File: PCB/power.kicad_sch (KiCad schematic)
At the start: 45 parts, among them Q1 AO3401A, U5 LM317_SOT-223, U6 LM317_SOT-223, U7 TPS65131RGE, U8 LM317_SOT-223, U9 LM337_SOT223

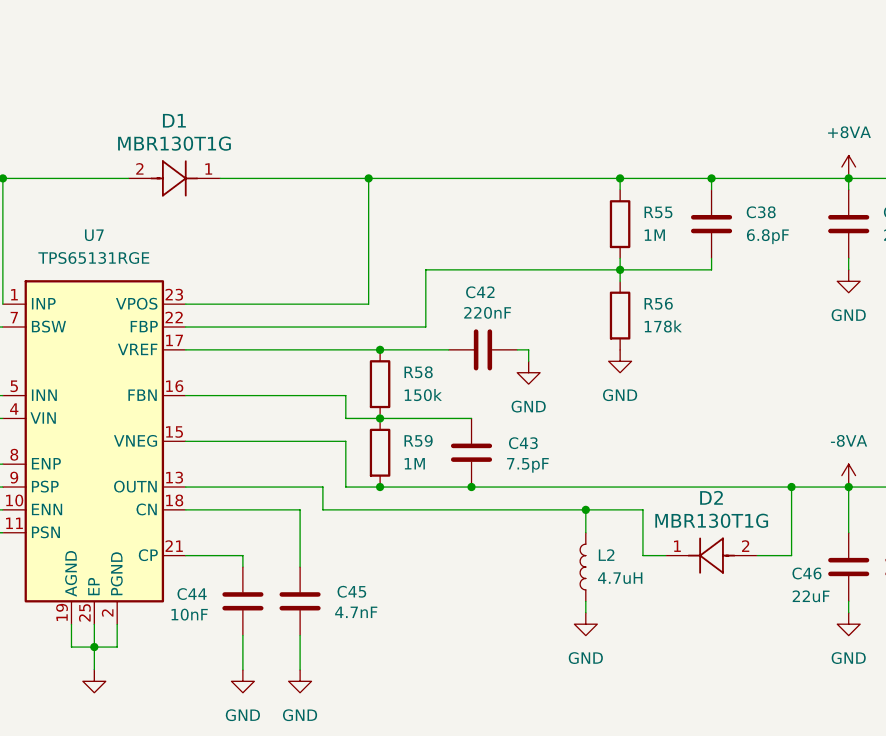
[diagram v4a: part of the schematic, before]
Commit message: Basic routing finished. Still missing some optimizing steps and DRC
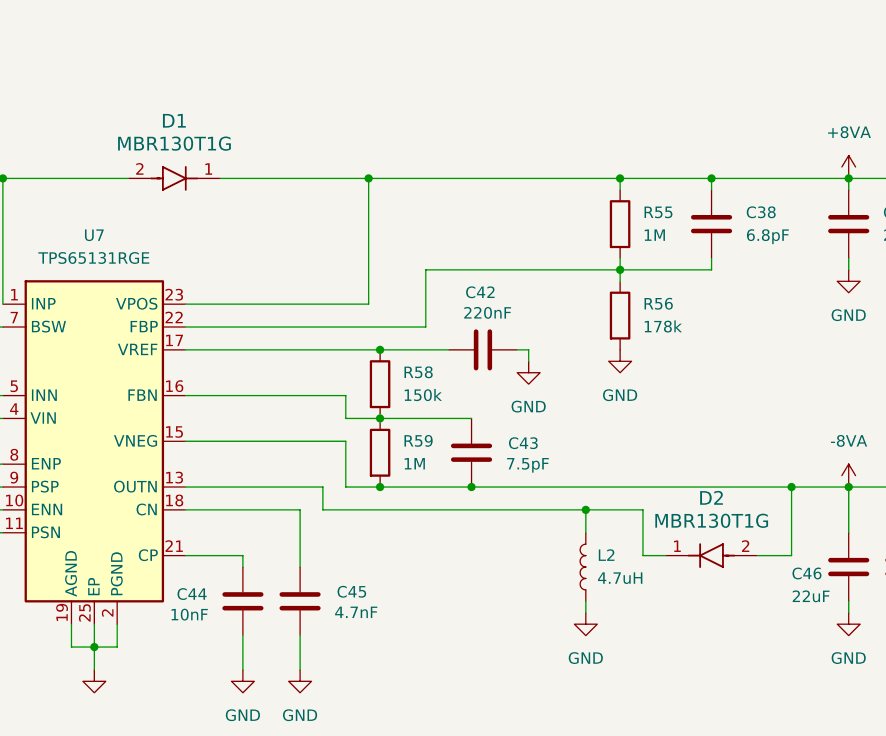
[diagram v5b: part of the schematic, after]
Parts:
- D1, D2: footprint SOD-123_425-04_ONS -> mahaudio KiCad Library:SOD-123_425-04_ONS; symbol mahaudio_kicad_lib:MBR130T1G -> mahaudio KiCad Library:MBR130T1G
- L1, L2: footprint LIB:WE-MAPI_4030 -> mahaudio KiCad Library:WE-MAPI_4030
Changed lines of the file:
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@@
 			)
 		)
-		(symbol "mahaudio_kicad_lib:MBR130T1G"
+		(symbol "mahaudio KiCad Library:MBR130T1G"
 			(pin_names
 				(offset 0.254)
@@
 			(in_bom yes)
 			(on_board yes)
-			(property "Reference" "CR"
-				(at 5.08 4.445 0)
+			(property "Reference" "D"
+				(at 5.08 -6.35 0)
 				(effects
 					(font
@@
 				)
 			)
-			(property "Footprint" "SOD-123_425-04_ONS"
+			(property "Footprint" "mahaudio KiCad Library:SOD-123_425-04_ONS"
 				(at 0 0 0)
 				(effects
@@
 				(polyline
 					(pts
-						(xy 3.81 -1.905) (xy 6.35 0)
+						(xy 3.81 -1.27) (xy 6.35 0)
 					)
 					(stroke
@@
 				(polyline
 					(pts
-						(xy 3.81 1.905) (xy 3.81 -1.905)
+						(xy 3.81 1.27) (xy 3.81 -1.27)
 					)
 					(stroke
@@
 				(polyline
 					(pts
-						(xy 6.35 -1.905) (xy 6.35 1.905)
+						(xy 6.35 -1.27) (xy 6.35 1.27)
 					)
 					(stroke
@@
 				(polyline
 					(pts
-						(xy 6.35 0) (xy 3.81 1.905)
+						(xy 6.35 0) (xy 3.81 1.27)
 					)
 					(stroke
@@
 			)
 		)
-		(property "Footprint" "LIB:WE-MAPI_4030"
+		(property "Footprint" "mahaudio KiCad Library:WE-MAPI_4030"
 			(at 156.21 76.2 0)
 			(effects
@@
 	)
 	(symbol
-		(lib_id "mahaudio_kicad_lib:MBR130T1G")
+		(lib_id "mahaudio KiCad Library:MBR130T1G")
 		(at 105.41 33.02 0)
 		(unit 1)
@@
 			)
 		)
-		(property "Footprint" "SOD-123_425-04_ONS"
+		(property "Footprint" "mahaudio KiCad Library:SOD-123_425-04_ONS"
 			(at 105.41 33.02 0)
 			(effects
@@
 	)
 	(symbol
-		(lib_id "mahaudio_kicad_lib:MBR130T1G")
+		(lib_id "mahaudio KiCad Library:MBR130T1G")
 		(at 175.26 74.93 180)
 		(unit 1)
@@
 			)
 		)
-		(property "Footprint" "SOD-123_425-04_ONS"
+		(property "Footprint" "mahaudio KiCad Library:SOD-123_425-04_ONS"
 			(at 175.26 74.93 0)
 			(effects
@@
 			)
 		)
-		(property "Footprint" "LIB:WE-MAPI_4030"
+		(property "Footprint" "mahaudio KiCad Library:WE-MAPI_4030"
 			(at 85.09 33.02 0)
 			(effects

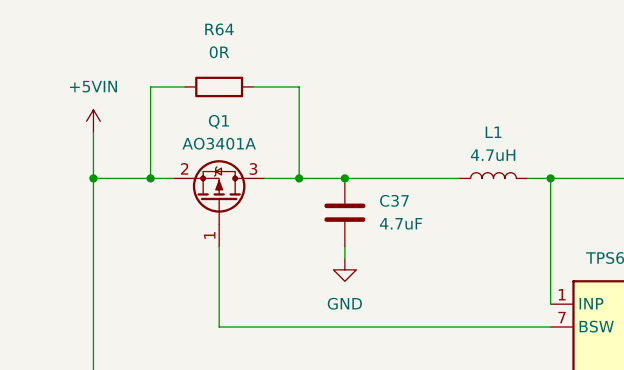
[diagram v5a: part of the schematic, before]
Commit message: Routing revised, added some missing parameters to components
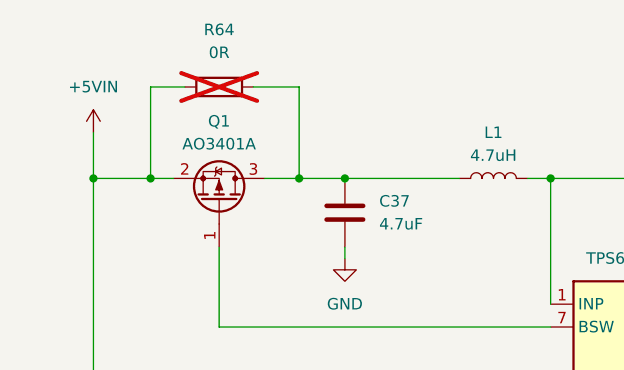
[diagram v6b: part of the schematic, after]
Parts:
- C21, C23, C24, C30, C44, C45, C50, C51: Tolerance (none) -> 10%; Voltage (none) -> 16V
- C22, C29, C41, C42, C48, C49: Tolerance (none) -> 10%; Voltage (none) -> 25V
- C37, C39, C40, C46, C47: Tolerance (none) -> 10%; Voltage (none) -> 10V
- C38, C43: Tolerance (none) -> 0.1pF; Voltage (none) -> 50V
- L1, L2: Tolerance (none) -> 20%
- R43, R44, R53, R54, R55, R56, R58, R59, R62, R63: Tolerance (none) -> 1%
- R57, R60, R61: Tolerance (none) -> 5%
- R64: now not fitted

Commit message: Updated PCB with digital traxce suggestions. Added JLCPCB Pns
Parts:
- C21, C23, C24, C30, C50, C51: JLCPCBPn (none) -> C15849
- C22, C29, C41, C48, C49: JLCPCBPn (none) -> C1525; Voltage 25V -> 16V
- C37, C40: JLCPCBPn (none) -> C19666
- C38: JLCPCBPn (none) -> C88896
- C39, C46, C47: JLCPCBPn (none) -> C84419
- C42: JLCPCBPn (none) -> C16772; Voltage 25V -> 16V
- C43: JLCPCBPn (none) -> C88938
- C44: JLCPCBPn (none) -> C15195; Voltage 16V -> 50V
- C45: JLCPCBPn (none) -> C1538; Voltage 16V -> 50V
- D1, D2: JLCPCBPn (none) -> C82461
- L1, L2: JLCPCBPn (none) -> C6707914
- Q1: JLCPCBPn (none) -> C15127
- R43, R53: JLCPCBPn (none) -> C274891
- R44, R54, R62, R63: JLCPCBPn (none) -> C25094
- R55, R59: JLCPCBPn (none) -> C26083
- R57: JLCPCBPn (none) -> C25076
- R58: JLCPCBPn (none) -> C25755
- R60, R61: JLCPCBPn (none) -> C416571; Tolerance 5% -> 1%
- U5, U6, U8: JLCPCBPn (none) -> C84244
- U7: JLCPCBPn (none) -> C87663
- U9: JLCPCBPn (none) -> C527400

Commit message: Changed resistor values to match JLCPCB + general board revision
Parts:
- R56: JLCPCBPn (none) -> C185459
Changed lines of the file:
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@@
+			)
+		)
+		(property "JLCPCBPn" "C185459"
+			(at 160.02 48.26 0)
+			(effects
+				(font
+					(size 1.27 1.27)
+				)
+				(hide yes)
 			)
 		)
